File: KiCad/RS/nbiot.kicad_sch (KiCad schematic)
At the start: 1 part, among them U8 ST87M01-1301

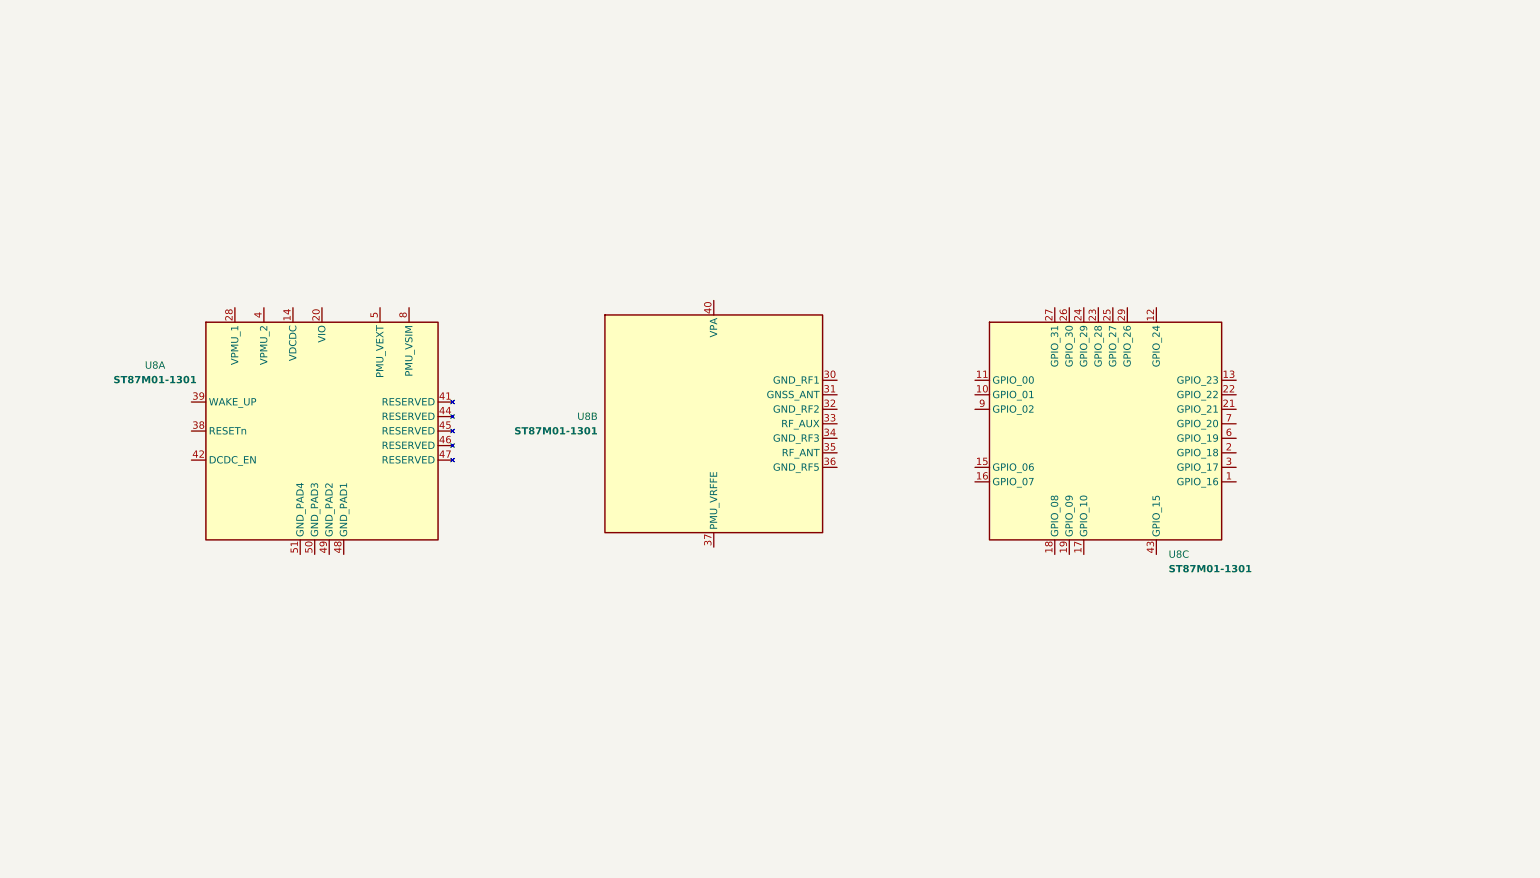
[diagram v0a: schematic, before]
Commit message: ADD: ST87M01-1301 Modem.
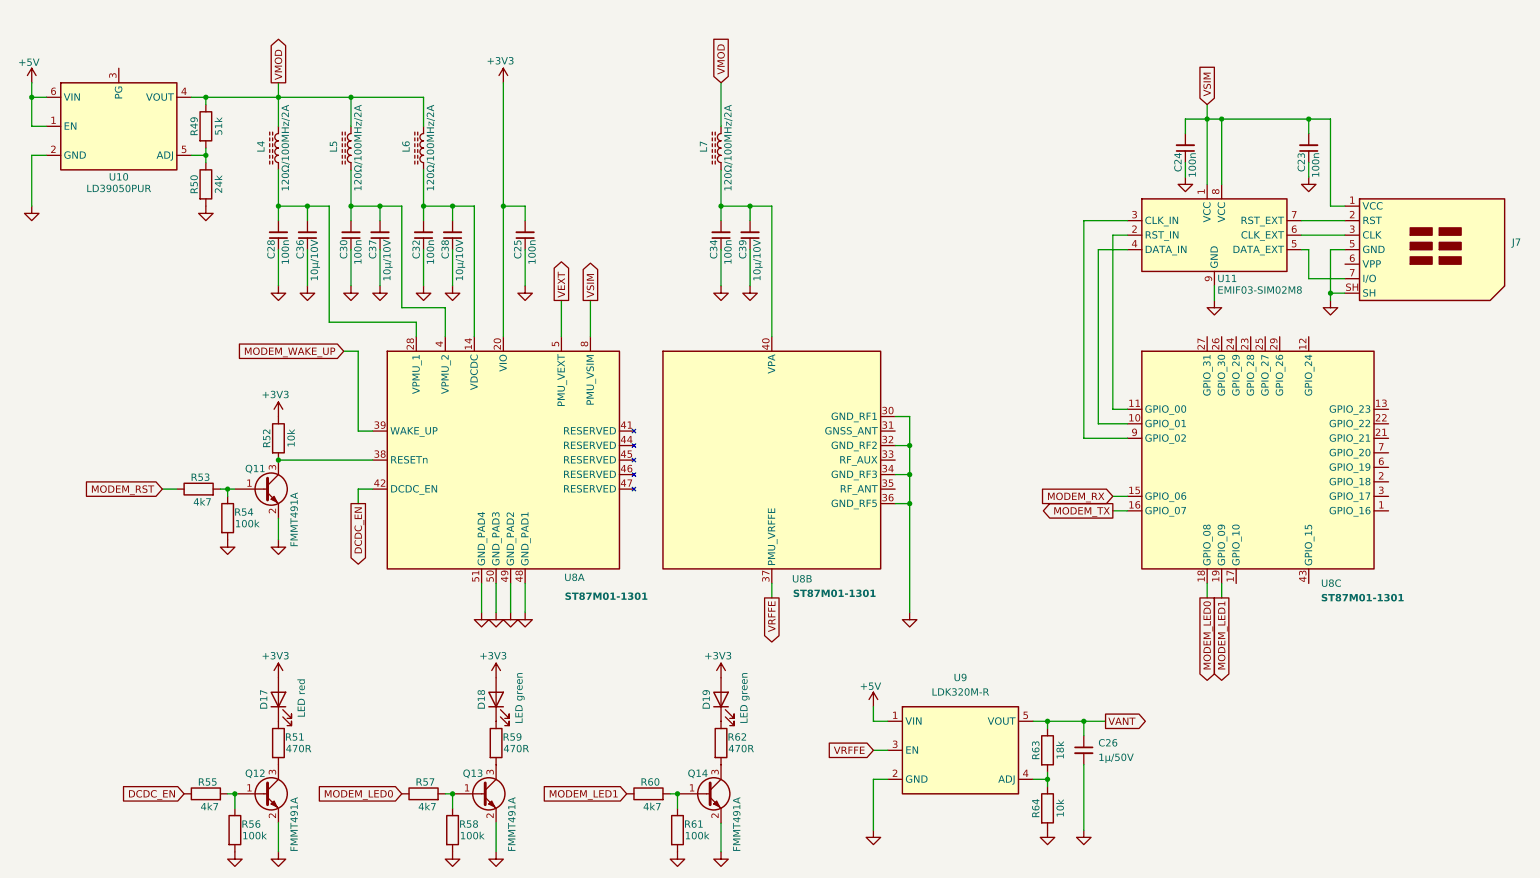
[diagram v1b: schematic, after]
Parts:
- added C23, C24, C25, C28, C30, C32, C34: 100n, Capacitor_SMD:C_0805_2012Metric_Pad1.18x1.45mm_HandSolder, symbol Device:C_Small
- added C26: 1μ/50V, Capacitor_SMD:C_0805_2012Metric_Pad1.18x1.45mm_HandSolder, symbol Device:C_Small
- added C36, C37, C38, C39: 10μ/10V, Capacitor_SMD:C_1206_3216Metric_Pad1.33x1.80mm_HandSolder, symbol Device:C_Small
- added D17: LED red, Diode_SMD:D_0805_2012Metric_Pad1.15x1.40mm_HandSolder, symbol Device:LED
- added D18, D19: LED green, Diode_SMD:D_0805_2012Metric_Pad1.15x1.40mm_HandSolder, symbol Device:LED
- added J7: SIM_Card_Shielded, symbol Connector:SIM_Card_Shielded
- added L4, L5, L6, L7: 120Ω/100MHz/2A, symbol Device:L_Ferrite
- added Q11, Q12, Q13, Q14: FMMT491A, Package_TO_SOT_SMD:SOT-23, symbol CustomSymbols:FMMT491A
- added R49: 51k, Resistor_SMD:R_0805_2012Metric_Pad1.20x1.40mm_HandSolder, symbol Device:R
- added R50: 24k, Resistor_SMD:R_0805_2012Metric_Pad1.20x1.40mm_HandSolder, symbol Device:R
- added R51, R59, R62: 470R, Resistor_SMD:R_0805_2012Metric_Pad1.20x1.40mm_HandSolder, symbol Device:R
- added R52, R64: 10k, Resistor_SMD:R_0805_2012Metric_Pad1.20x1.40mm_HandSolder, symbol Device:R
- added R53, R55, R57, R60: 4k7, Resistor_SMD:R_0805_2012Metric_Pad1.20x1.40mm_HandSolder, symbol Device:R
- added R54, R56, R58, R61: 100k, Resistor_SMD:R_0805_2012Metric_Pad1.20x1.40mm_HandSolder, symbol Device:R
- added R63: 18k, Resistor_SMD:R_0805_2012Metric_Pad1.20x1.40mm_HandSolder, symbol Device:R
- added U10: LD39050PUR, Package_DFN_QFN:DFN-6-1EP_3x3mm_P0.95mm_EP1.7x2.6mm, symbol CodeDog:LD39050PUR
- added U11: EMIF03-SIM02M8, symbol CodeDog:EMIF03-SIM02M8
- added U9: LDK320M-R, Package_TO_SOT_SMD:SOT-23-5_HandSoldering, symbol CodeDog:LDK320M-R
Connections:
- net GND: now reaches U8.30 (GND_RF1)
- net GND: now also U8.32 (GND_RF2), U8.34 (GND_RF3), U8.36 (GND_RF5), U8.48 (GND_PAD1), U8.49 (GND_PAD2), U8.50 (GND_PAD3), U8.51 (GND_PAD4), C23.1, C24.1, C25.1, C26.2, C28.1, C30.1, C32.1, C34.1, C36.1, C37.1, C38.1, C39.1, J7.5 (GND), J7.SH, Q11.2 (E), Q12.2 (E), Q13.2 (E), Q14.2 (E), R50.2, R54.2, R56.2, R58.2, R61.2, R64.2, U10.2 (GND), U11.9 (GND), U9.2 (GND)
- net VRFFE: now reaches U8.37 (PMU_VRFFE)
- net VRFFE: now also U9.3 (EN)
- net at U8.40 (VPA): now also C34.2, C39.2, L7.2
- net at U8.14 (VDCDC): now also C32.2, C38.2, L6.2
- net +3V3: now reaches U8.20 (VIO)
- net +3V3: now also C25.2, D17.2 (A), D18.2 (A), D19.2 (A), R52.1
- net at U8.28 (VPMU_1): now also C28.2, C36.2, L4.2
- net at U8.38 (RESETn): now also Q11.3 (C), R52.2
- net MODEM_WAKE_UP: now reaches U8.39 (WAKE_UP)
- net at U8.4 (VPMU_2): now also C30.2, C37.2, L5.2
- net DCDC_EN: now reaches U8.42 (DCDC_EN)
- net DCDC_EN: now also R55.1
- net VEXT: now reaches U8.5 (PMU_VEXT)
- net VSIM: now reaches U8.8 (PMU_VSIM)
- net VSIM: now also C23.2, C24.2, J7.1 (VCC), U11.1 (VCC), U11.8 (VCC)
- net at U8.10 (GPIO_01): now also U11.4 (DATA_IN)
- net at U8.11 (GPIO_00): now also U11.2 (RST_IN)
- net MODEM_RX: now reaches U8.15 (GPIO_06)
- net MODEM_TX: now reaches U8.16 (GPIO_07)
- net MODEM_LED0: now reaches U8.18 (GPIO_08)
- net MODEM_LED0: now also R57.1
- net MODEM_LED1: now reaches U8.19 (GPIO_09)
- net MODEM_LED1: now also R60.1
- net at U8.9 (GPIO_02): now also U11.3 (CLK_IN)
- new net: D19.1 (K), R62.1
- new net: Q14.3 (C), R62.2
- new net: Q13.1 (B), R57.2, R58.1
- new net: D17.1 (K), R51.1
- new net: Q12.3 (C), R51.2
- new net: Q11.1 (B), R53.2, R54.1
- new net: Q12.1 (B), R55.2, R56.1
- new net: J7.7 (I/O), U11.5 (DATA_EXT)
- new net: J7.3 (CLK), U11.6 (CLK_EXT)
- new net: J7.2 (RST), U11.7 (RST_EXT)
- new net: R49.2, R50.1, U10.5 (ADJ)
- new net: R63.2, R64.1, U9.4 (ADJ)
- new net: Q14.1 (B), R60.2, R61.1
- new net: D18.1 (K), R59.1
- new net: Q13.3 (C), R59.2
- new net +5V: U10.1 (EN), U10.6 (VIN), U9.1 (VIN)
- new net MODEM_RST: R53.1
- new net VANT: C26.1, R63.1, U9.5 (VOUT)
- new net VMOD: L4.1, L5.1, L6.1, L7.1, R49.1, U10.4 (VOUT)
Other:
- moved on the sheet: U8A, U8B, U8C

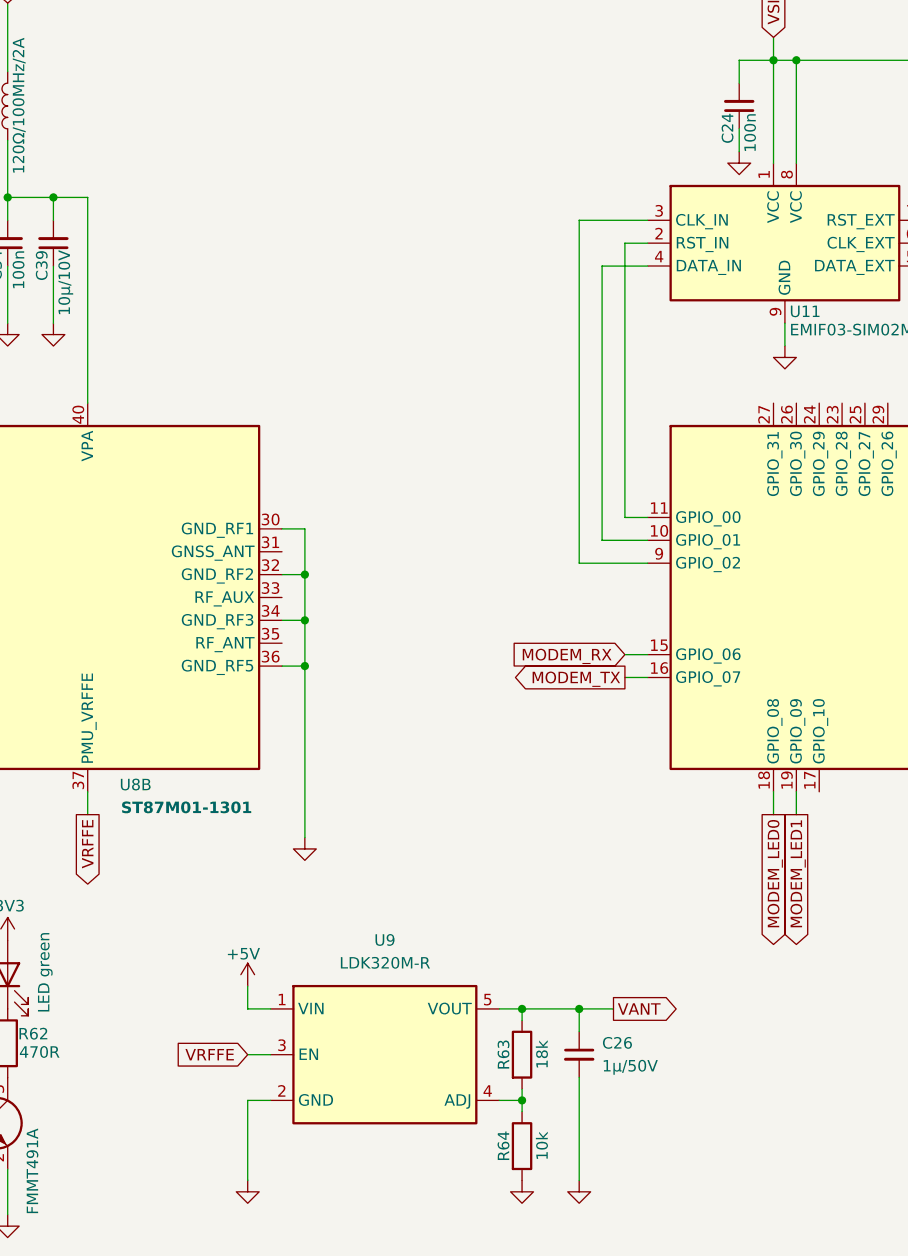
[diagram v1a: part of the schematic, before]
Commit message: ADD: U.FL sockets circuits.
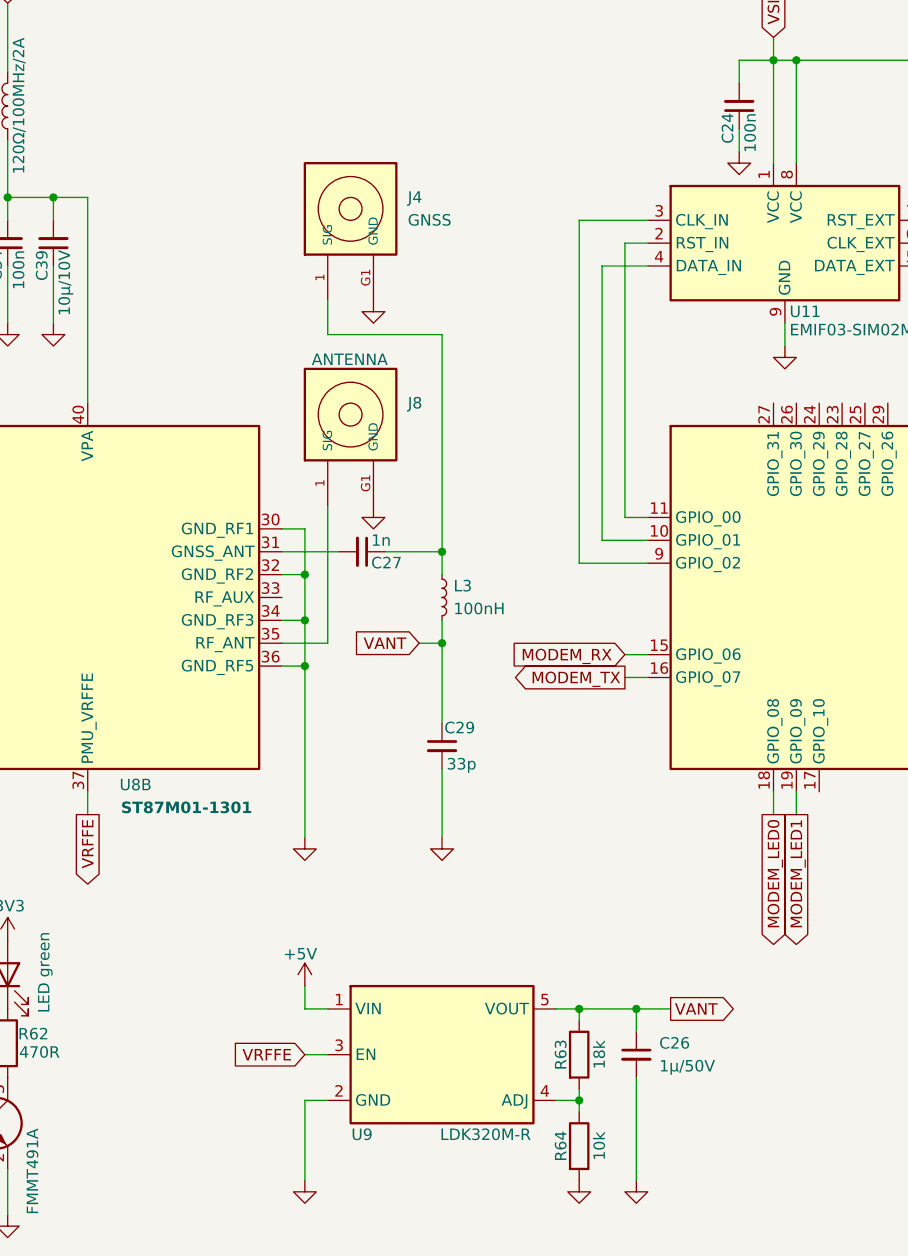
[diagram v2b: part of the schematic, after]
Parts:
- added C27: 1n, Capacitor_SMD:C_0805_2012Metric_Pad1.18x1.45mm_HandSolder, symbol Device:C_Small
- added C29: 33p, Capacitor_SMD:C_0805_2012Metric_Pad1.18x1.45mm_HandSolder, symbol Device:C_Small
- added J4: GNSS, CodeDog:TE_1909763-1, symbol CodeDog:1909763-1
- added J8: ANTENNA, CodeDog:TE_1909763-1, symbol CodeDog:1909763-1
- added L3: 100nH, Inductor_SMD:L_0805_2012Metric_Pad1.05x1.20mm_HandSolder, symbol Device:L_Small
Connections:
- net GND: now also C29.2, J4.G1 (GND), J8.G1 (GND)
- net VANT: now also C29.1, L3.2
- net at U8.31 (GNSS_ANT): now also C27.2
- net at U8.35 (RF_ANT): now also J8.1 (SIG)
- new net: C27.1, J4.1 (SIG), L3.1
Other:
- moved on the sheet: C26, R63, R64, U9

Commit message: FIX: BOM, SCH.
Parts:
- removed C36, C37, C38: 10μ/10V, Capacitor_SMD:C_1206_3216Metric_Pad1.33x1.80mm_HandSolder, symbol Device:C_Small
- removed Q11, Q12, Q13, Q14: FMMT491A, Package_TO_SOT_SMD:SOT-23, symbol CustomSymbols:FMMT491A
- added C26, C28, C30: 10μ/10V, Capacitor_SMD:C_1206_3216Metric_Pad1.33x1.80mm_HandSolder, symbol Device:C_Small
- added Q10, Q11, Q12, Q9: BC817, Package_TO_SOT_SMD:SOT-23, symbol Transistor_BJT:BC817
- C33: renamed from C39; Mfg Part # GMT31X7R106K10NT2 -> GMC31Y5V106Z10NT; URL https://www.digikey.pl/en/products/detail/taiyo-yuden/UMK10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 -> https://www.digikey.pl/en/products/detail/cal-chip-electron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
- C34: renamed from C27; footprint Capacitor_SMD:C_0805_2012Metric_Pad1.18x1.45mm_HandSolder -> Capacitor_SMD:C_0402_1005Metric; Mfg Part # CC0805MRX7R0BB102 -> C0402C102K1GACAUTO; URL https://www.digikey.pl/en/products/detail/yageo/CC0805MRX7R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 -> https://www.digikey.pl/en/products/detail/kemet/C0402C102K1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
- C35: renamed from C29; footprint Capacitor_SMD:C_0805_2012Metric_Pad1.18x1.45mm_HandSolder -> Capacitor_SMD:C_0402_1005Metric; Mfg Part # CC0805MRX7R0BB102 -> CL05C330JB5NNNC; URL https://www.digikey.pl/en/products/detail/yageo/CC0805MRX7R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 -> https://www.digikey.pl/en/products/detail/samsung-electro-m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
- C36: renamed from C26; Mfg Part # UMK107BJ105KA-T -> GMC21X7R105K50NT; URL https://www.digikey.pl/en/products/detail/taiyo-yuden/UMK10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 -> https://www.digikey.pl/en/products/detail/cal-chip-electron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
- D17: Mfg Part # B1701NG--20D000314U1930 -> B1701USD-20D000114U1930; URL (none) -> https://www.digikey.pl/en/products/detail/harvatek-corporat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
- D18, D19: URL (none) -> https://www.digikey.pl/en/products/detail/harvatek-corporat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
- J8: renamed from J7; value SIM_Card_Shielded -> SIM; footprint (none) -> Connector_Card:nanoSIM_GCT_SIM8060-6-0-14-00; Mfg Part # (none) -> SIM8060-6-0-14-00-A; URL (none) -> https://www.digikey.pl/en/products/detail/gct/SIM8060-6-0-1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
- L7: renamed from L3; footprint Inductor_SMD:L_0805_2012Metric_Pad1.05x1.20mm_HandSolder -> Inductor_SMD:L_0402_1005Metric; Mfg Part # LQW2BASR10J00L -> LQW15ANR10J0ZD; URL https://www.digikey.pl/en/products/detail/murata-electronics/LQW2BASR10J00L/2625449 -> https://www.digikey.pl/en/products/detail/murata-electronics/LQW15ANR10J0ZD/8323944
- R54: renamed from R49; Mfg Part # CR0805JB10KS01 -> ERA-6AEB513V; URL https://www.digikey.pl/en/products/detail/nextgen-component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 -> https://www.digikey.pl/en/products/detail/panasonic-industr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
- R55: renamed from R50; Mfg Part # CR0805JB10KS01 -> RT0805BRD0724KL; URL https://www.digikey.pl/en/products/detail/nextgen-component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 -> https://www.digikey.pl/en/products/detail/yageo/RT0805BRD07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
- R62: renamed from R63; Mfg Part # CR0805JB10KS01 -> ERA-6AEB183V; URL https://www.digikey.pl/en/products/detail/nextgen-component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 -> https://www.digikey.pl/en/products/detail/panasonic-industr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
- R66: renamed from R64; Mfg Part # CR0805JB10KS01 -> RG2012P-103-B-T5; URL https://www.digikey.pl/en/products/detail/nextgen-component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 -> https://www.digikey.pl/en/products/detail/susumu/RG2012P-10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
- U9: renamed from U11; footprint (none) -> CodeDog:MICROQFN_1P7X1P5_STM; Mfg Part # (none) -> EMIF03-SIM02M8; URL (none) -> https://www.digikey.pl/en/products/detail/stmicroelectronic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
- renumbered C24 to C23, C23 to C24, C28 to C25, C30 to C27, C32 to C29, C25 to C31, C34 to C32, J4 to J7, J8 to J9, L4 to L3, L5 to L4, L6 to L5, L7 to L6, R52 to R56, R53 to R57, R54 to R58, R51 to R59, R59 to R60, R62 to R61, R55 to R63, R57 to R64, R60 to R65, R56 to R67, R58 to R68, R61 to R69, U8 to U10, U9 to U11, U10 to U8
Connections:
- net GND: now also C26.1, C28.1, C30.1, Q10.2 (E), Q11.2 (E), Q12.2 (E), Q9.2 (E)
- net at R61.2: now also Q12.3 (C)
- net at R64.2, R68.1: now also Q11.1 (B)
- net at C25.2, L3.2, U10.28 (VPMU_1): now also C26.2
- net at R59.2: now also Q10.3 (C)
- net at R56.2, U10.38 (RESETn): now also Q9.3 (C)
- net at R57.2, R58.1: now also Q9.1 (B)
- net at R63.2, R67.1: now also Q10.1 (B)
- net at C29.2, L5.2, U10.14 (VDCDC): now also C30.2
- net at R65.2, R69.1: now also Q12.1 (B)
- net at C27.2, L4.2, U10.4 (VPMU_2): now also C28.2
- net at R60.2: now also Q11.3 (C)
- net VMOD_PG: now reaches U8.3 (PG)
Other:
- company: (none) -> CodeDog
- title: (none) -> Remote Sensor Module: NBIOT
- moved on the sheet: C23, C24, C25, C27, C29, C31, C32, C33, C34, C35, C36, D18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

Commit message: ADD: RF connections.
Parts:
- L3, L4, L5: footprint (none) -> Inductor_SMD:L_0805_2012Metric_Pad1.05x1.20mm_HandSolder
- L6: footprint (none) -> Inductor_SMD:L_0805_2012Metric_Pad1.05x1.20mm_HandSolder; Manufacturer_Part_Number 1-2176744-5 -> (none); Mfg Part # (none) -> 1-2176744-5; URL (none) -> https://www.digikey.pl/en/products/detail/te-connectivity-p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
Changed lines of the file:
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@@
 			)
 		)
-		(property "Footprint" ""
+		(property "Footprint" "Inductor_SMD:L_0805_2012Metric_Pad1.05x1.20mm_HandSolder"
 			(at 62.23 40.64 0)
 			(hide yes)
@@
 			)
 		)
-		(property "Footprint" ""
+		(property "Footprint" "Inductor_SMD:L_0805_2012Metric_Pad1.05x1.20mm_HandSolder"
 			(at 74.93 40.64 0)
 			(hide yes)
@@
 			)
 		)
-		(property "Footprint" ""
+		(property "Footprint" "Inductor_SMD:L_0805_2012Metric_Pad1.05x1.20mm_HandSolder"
 			(at 87.63 40.64 0)
 			(hide yes)
@@
 			)
 		)
-		(property "Footprint" ""
+		(property "Footprint" "Inductor_SMD:L_0805_2012Metric_Pad1.05x1.20mm_HandSolder"
 			(at 139.7 40.64 0)
 			(hide yes)
@@
 			)
 		)
-		(property "Manufacturer_Part_Number" "1-2176744-5"
+		(property "Mfg Part #" "1-2176744-5"
 			(at 139.7 40.64 0)
 			(hide yes)
@@
 			(at 139.7 40.64 90)
 			(hide yes)
+			(show_name no)
+			(do_not_autoplace no)
+			(effects
+				(font
+					(size 1.27 1.27)
+				)
+			)
+		)
+		(property "URL" "https://www.digikey.pl/en/products/detail/te-connectivity-passive-product/1-2176744-5/25589478"
+			(at 139.7 40.64 90)
+			(hide yes)
